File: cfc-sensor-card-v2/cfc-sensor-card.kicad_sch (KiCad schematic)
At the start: 8 parts, among them J1 TFM-120-01-L-D-RA, J2 J-SAMTEC-TFM-110-X1-XXX-D-RA

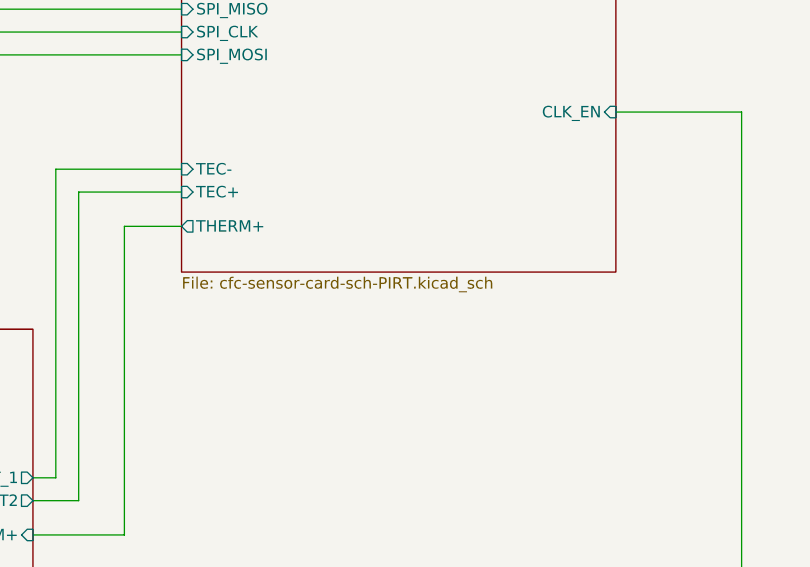
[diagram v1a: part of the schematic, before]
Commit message: Updated OPD on sensor card
updated OPD on sensor card to match protocard. Finished placement on PCB.
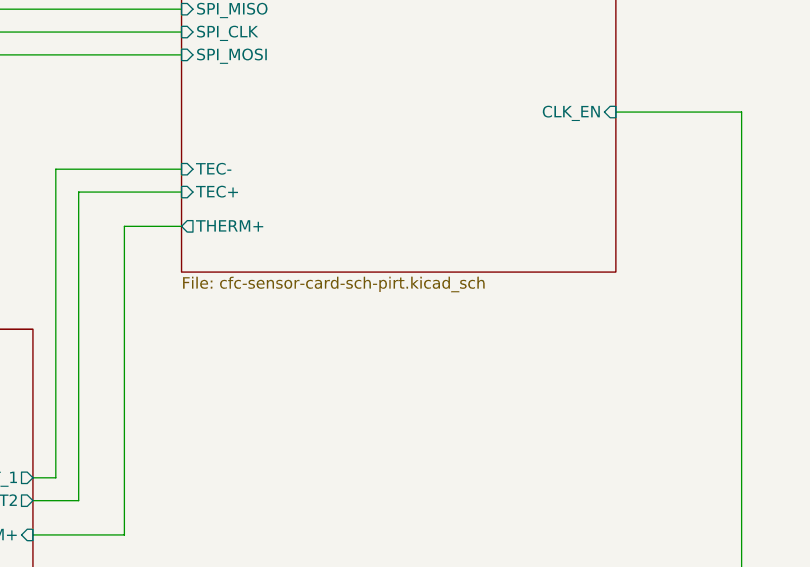
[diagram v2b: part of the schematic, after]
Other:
- sheet PIRT: file cfc-sensor-card-sch-PIRT.kicad_sch -> cfc-sensor-card-sch-pirt.kicad_sch
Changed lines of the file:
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@@
 			)
 		)
-		(property "Sheetfile" "cfc-sensor-card-sch-PIRT.kicad_sch"
+		(property "Sheetfile" "cfc-sensor-card-sch-pirt.kicad_sch"
 			(at 243.84 152.908 0)
 			(show_name no)

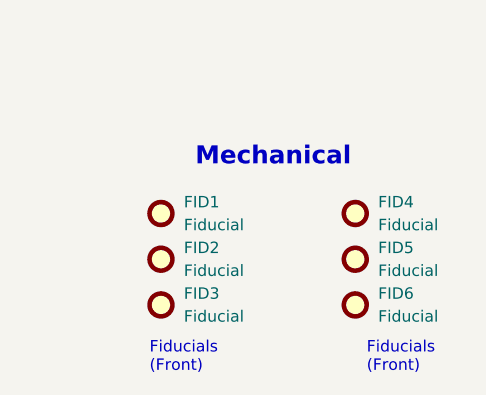
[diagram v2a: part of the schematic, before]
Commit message: Update
Updated BOM, couple of fixes on OPD. Minor routing and layout changes. Removed logic gates from sensor card.
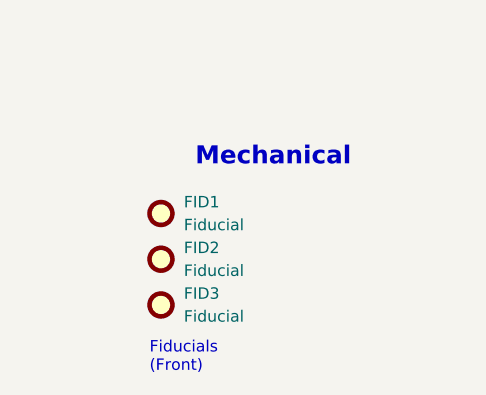
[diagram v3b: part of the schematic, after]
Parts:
- removed FID4, FID5, FID6: Fiducial, Fiducial:Fiducial_1mm_Mask2mm, symbol Mechanical:Fiducial
